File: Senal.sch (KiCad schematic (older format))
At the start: 19 parts, among them IC1 AG849, IC2 AD5933, P1 GSG-RF-CONN, P2 GSG-RF-CONN, P3 CONN_02X04, P4 CONN_01X01, U1 AD8606

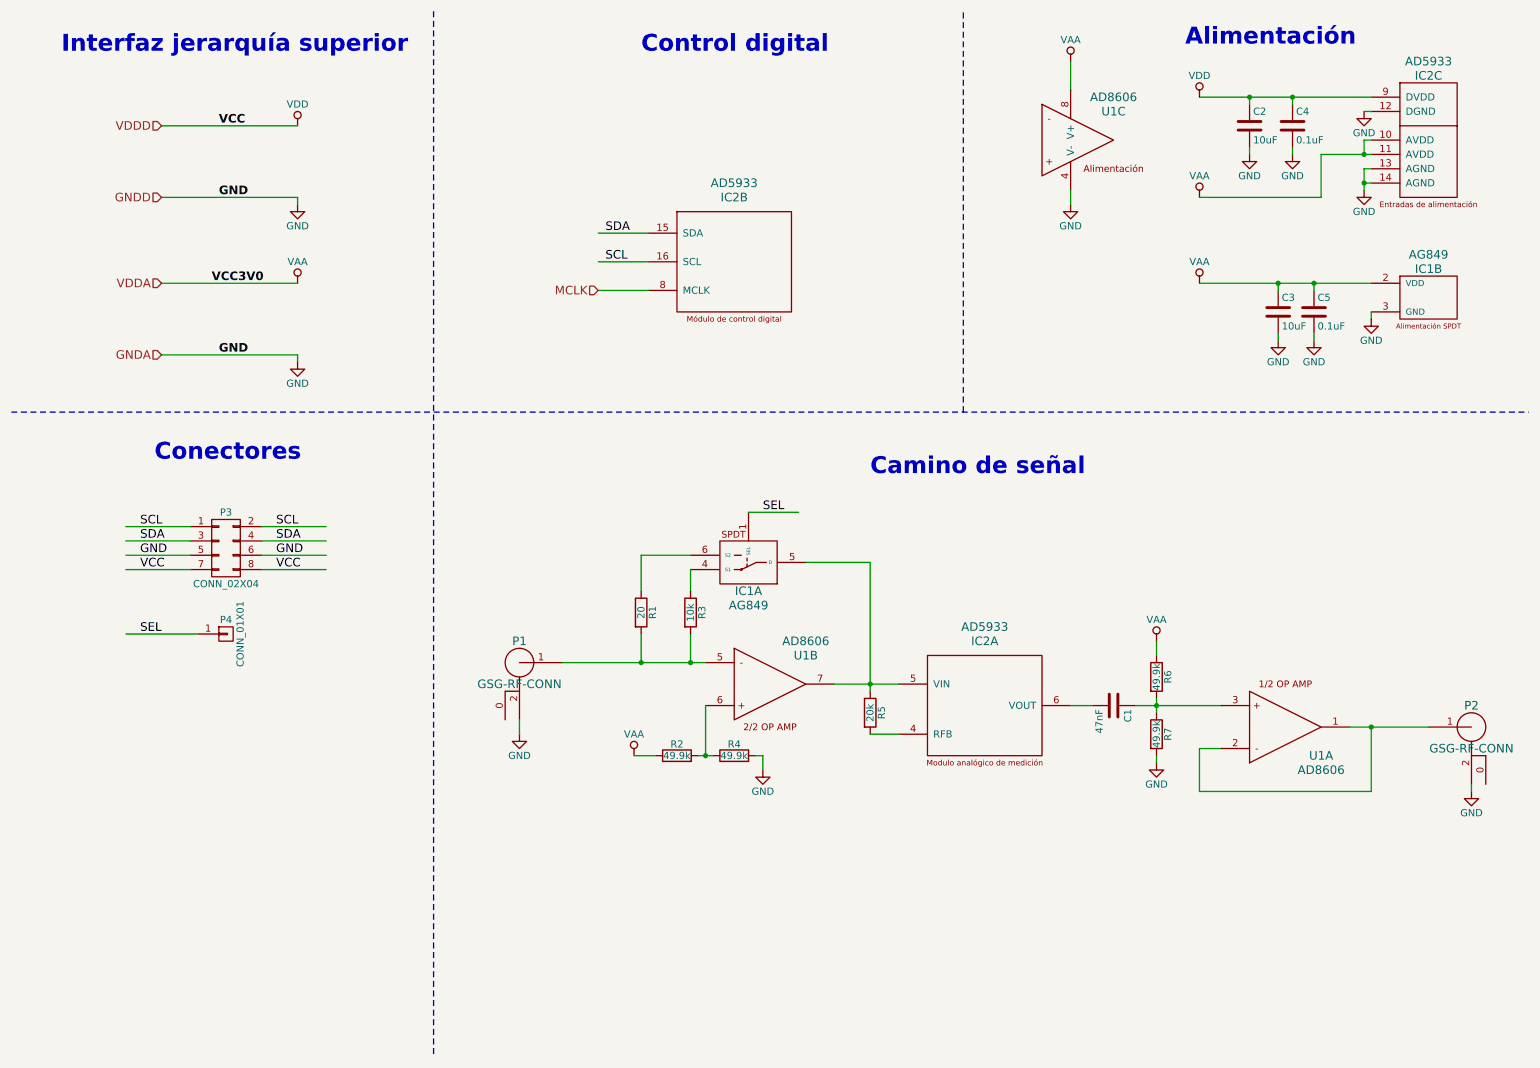
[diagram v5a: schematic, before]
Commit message: Footprints creados y linkeados. Listo para proceder al PCB. Todas las DRC dan OK
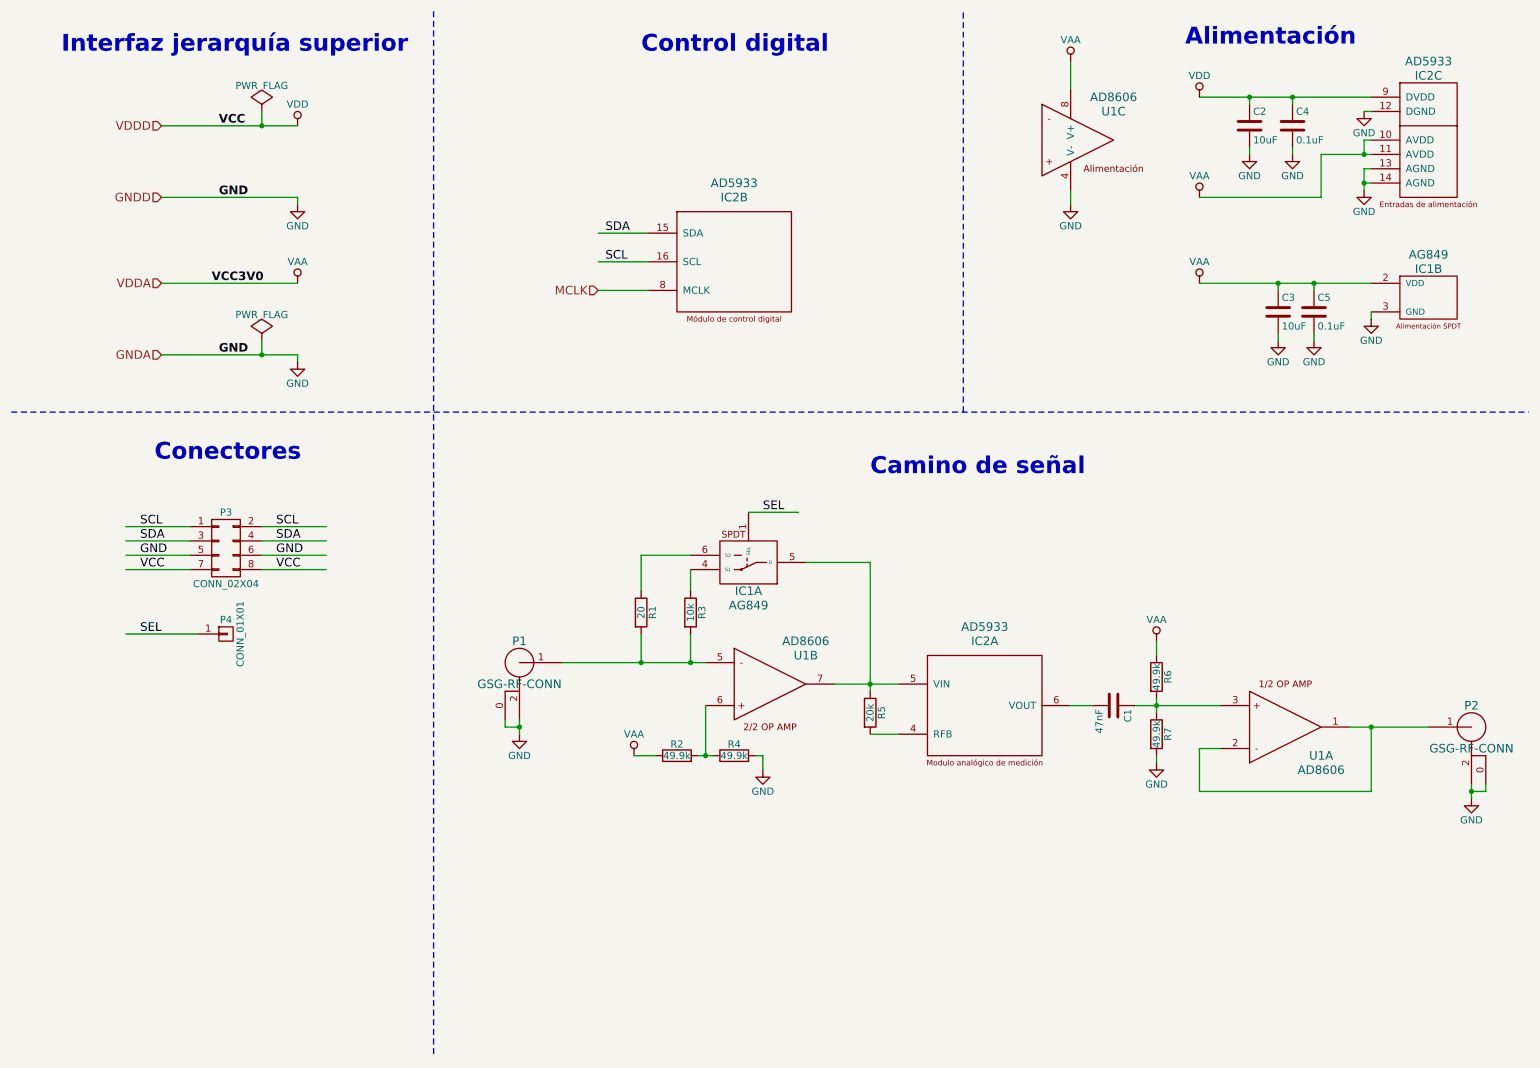
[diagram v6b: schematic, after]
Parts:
- C1, C2, C3, C4, C5: footprint (none) -> Capacitors_SMD:C_0805
- IC1: footprint (none) -> TO_SOT_Packages_SMD:SC-70-6
- IC2: footprint (none) -> Housings_SSOP:SSOP-16_5.3x6.2mm_Pitch0.65mm
- P1, P2: footprint (none) -> SMA_EDGE:SMA_EDGE
- P3: footprint (none) -> Pin_Headers:Pin_Header_Straight_2x04
- P4: footprint (none) -> Pin_Headers:Pin_Header_Straight_1x01
- R1, R2, R3, R4, R5, R6, R7: footprint (none) -> Resistors_SMD:R_0805
- U1: footprint (none) -> Housings_SSOP:MSOP-8_3x3mm_Pitch0.65mm
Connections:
- wire segments 68 -> 74
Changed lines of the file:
@@
 LIBS:PMOD_IA
 LIBS:SMA
+LIBS:sma2
 LIBS:proyectoDCI-cache
 EELAYER 25 0
@@
 F 0 "IC2" H 10450 1850 60  0000 C CNN
 F 1 "AD5933" H 10450 1950 60  0000 C CNN
-F 2 "" H 10450 1400 60  0001 C CNN
+F 2 "Housings_SSOP:SSOP-16_5.3x6.2mm_Pitch0.65mm" H 10450 1400 60  0001 C CNN
 F 3 "" H 10450 1400 60  0001 C CNN
 	3    10450 1400
@@
 F 0 "C2" H 9225 1400 50  0000 L CNN
 F 1 "10uF" H 9225 1200 50  0000 L CNN
-F 2 "" H 9238 1150 50  0000 C CNN
+F 2 "Capacitors_SMD:C_0805" H 9238 1150 50  0001 C CNN
 F 3 "" H 9200 1300 50  0000 C CNN
 	1    9200 1300
@@
 F 0 "C4" H 9525 1400 50  0000 L CNN
 F 1 "0.1uF" H 9525 1200 50  0000 L CNN
-F 2 "" H 9538 1150 50  0000 C CNN
+F 2 "Capacitors_SMD:C_0805" H 9538 1150 50  0001 C CNN
 F 3 "" H 9500 1300 50  0000 C CNN
 	1    9500 1300
@@
 F 0 "IC2" H 5600 2700 60  0000 C CNN
 F 1 "AD5933" H 5600 2800 60  0000 C CNN
-F 2 "" H 5600 2250 60  0001 C CNN
+F 2 "Housings_SSOP:SSOP-16_5.3x6.2mm_Pitch0.65mm" H 5600 2250 60  0001 C CNN
 F 3 "" H 5600 2250 60  0001 C CNN
 	2    5600 2250
@@
 F 0 "IC2" H 7350 5800 60  0000 C CNN
 F 1 "AD5933" H 7350 5900 60  0000 C CNN
-F 2 "" H 7350 5350 60  0001 C CNN
+F 2 "Housings_SSOP:SSOP-16_5.3x6.2mm_Pitch0.65mm" H 7350 5350 60  0001 C CNN
 F 3 "" H 7350 5350 60  0001 C CNN
 	1    7350 5350
@@
 F 0 "U1" H 8250 1600 60  0000 C CNN
 F 1 "AD8606" H 8250 1700 60  0000 C CNN
-F 2 "" H 8000 1400 60  0001 C CNN
+F 2 "Housings_SSOP:MSOP-8_3x3mm_Pitch0.65mm" H 8000 1400 60  0001 C CNN
 F 3 "" H 8000 1400 60  0001 C CNN
 	3    8000 1400
@@
 F 0 "IC1" H 10450 2700 60  0000 C CNN
 F 1 "AG849" H 10450 2800 60  0000 C CNN
-F 2 "" H 10450 2500 60  0001 C CNN
+F 2 "TO_SOT_Packages_SMD:SC-70-6" H 10450 2500 60  0001 C CNN
 F 3 "" H 10450 2500 60  0001 C CNN
 	2    10450 2500
@@
 F 0 "C3" H 9425 2700 50  0000 L CNN
 F 1 "10uF" H 9425 2500 50  0000 L CNN
-F 2 "" H 9438 2450 50  0000 C CNN
+F 2 "Capacitors_SMD:C_0805" H 9438 2450 50  0001 C CNN
 F 3 "" H 9400 2600 50  0000 C CNN
 	1    9400 2600
@@
 F 0 "C5" H 9675 2700 50  0000 L CNN
 F 1 "0.1uF" H 9675 2500 50  0000 L CNN
-F 2 "" H 9688 2450 50  0000 C CNN
+F 2 "Capacitors_SMD:C_0805" H 9688 2450 50  0001 C CNN
 F 3 "" H 9650 2600 50  0000 C CNN
 	1    9650 2600
@@
 F 0 "U1" H 9700 5700 60  0000 C CNN
 F 1 "AD8606" H 9700 5800 60  0000 C CNN
-F 2 "" H 9450 5500 60  0001 C CNN
+F 2 "Housings_SSOP:MSOP-8_3x3mm_Pitch0.65mm" H 9450 5500 60  0001 C CNN
 F 3 "" H 9450 5500 60  0001 C CNN
 	1    9450 5500
@@
 F 0 "U1" H 6100 5400 60  0000 C CNN
 F 1 "AD8606" H 6100 5500 60  0000 C CNN
-F 2 "" H 5850 5200 60  0001 C CNN
+F 2 "Housings_SSOP:MSOP-8_3x3mm_Pitch0.65mm" H 5850 5200 60  0001 C CNN
 F 3 "" H 5850 5200 60  0001 C CNN
 	2    5850 5200
@@
 F 0 "R5" V 6630 5400 50  0000 C CNN
 F 1 "20k" V 6550 5400 50  0000 C CNN
-F 2 "" V 6480 5400 50  0000 C CNN
+F 2 "Resistors_SMD:R_0805" V 6480 5400 50  0001 C CNN
 F 3 "" H 6550 5400 50  0000 C CNN
 	1    6550 5400
@@
 F 0 "R6" V 8630 5150 50  0000 C CNN
 F 1 "49.9k" V 8550 5150 50  0000 C CNN
-F 2 "" V 8480 5150 50  0000 C CNN
+F 2 "Resistors_SMD:R_0805" V 8480 5150 50  0001 C CNN
 F 3 "" H 8550 5150 50  0000 C CNN
 	1    8550 5150
@@
 F 0 "R7" V 8630 5550 50  0000 C CNN
 F 1 "49.9k" V 8550 5550 50  0000 C CNN
-F 2 "" V 8480 5550 50  0000 C CNN
+F 2 "Resistors_SMD:R_0805" V 8480 5550 50  0001 C CNN
 F 3 "" H 8550 5550 50  0000 C CNN
 	1    8550 5550
@@
 F 0 "C1" H 8275 5450 50  0000 L CNN
 F 1 "47nF" H 8275 5250 50  0000 L CNN
-F 2 "" H 8288 5200 50  0000 C CNN
+F 2 "Capacitors_SMD:C_0805" H 8288 5200 50  0001 C CNN
 F 3 "" H 8250 5350 50  0000 C CNN
 	1    8250 5350
@@
 F 0 "P2" H 10750 5650 60  0000 C CNN
 F 1 "GSG-RF-CONN" H 10750 5350 60  0000 C CNN
-F 2 "" H 10750 5500 60  0000 C CNN
+F 2 "SMA_EDGE:SMA_EDGE" H 10750 5500 60  0001 C CNN
 F 3 "" H 10750 5500 60  0000 C CNN
 	1    10750 5500
@@
 L GND #PWR012
 U 1 1 582FC324
-P 10750 5950
-F 0 "#PWR012" H 10750 5700 50  0001 C CNN
-F 1 "GND" H 10750 5800 50  0000 C CNN
-F 2 "" H 10750 5950 50  0000 C CNN
-F 3 "" H 10750 5950 50  0000 C CNN
-	1    10750 5950
+P 10750 6000
+F 0 "#PWR012" H 10750 5750 50  0001 C CNN
+F 1 "GND" H 10750 5850 50  0000 C CNN
+F 2 "" H 10750 6000 50  0000 C CNN
+F 3 "" H 10750 6000 50  0000 C CNN
+	1    10750 6000
 	1    0    0    -1
 $EndComp
@@
 F 0 "R2" V 5280 5700 50  0000 C CNN
 F 1 "49.9k" V 5200 5700 50  0000 C CNN
-F 2 "" V 5130 5700 50  0000 C CNN
+F 2 "Resistors_SMD:R_0805" V 5130 5700 50  0001 C CNN
 F 3 "" H 5200 5700 50  0000 C CNN
 	1    5200 5700
@@
 F 0 "R4" V 5680 5700 50  0000 C CNN
 F 1 "49.9k" V 5600 5700 50  0000 C CNN
-F 2 "" V 5530 5700 50  0000 C CNN
+F 2 "Resistors_SMD:R_0805" V 5530 5700 50  0001 C CNN
 F 3 "" H 5600 5700 50  0000 C CNN
 	1    5600 5700
@@
 F 0 "P1" H 4100 5200 60  0000 C CNN
 F 1 "GSG-RF-CONN" H 4100 4900 60  0000 C CNN
-F 2 "" H 4100 5050 60  0000 C CNN
+F 2 "SMA_EDGE:SMA_EDGE" H 4100 5050 60  0001 C CNN
 F 3 "" H 4100 5050 60  0000 C CNN
 	1    4100 5050
@@
 F 0 "IC1" H 5700 4550 60  0000 C CNN
 F 1 "AG849" H 5700 4650 60  0000 C CNN
-F 2 "" H 5700 4350 60  0001 C CNN
+F 2 "TO_SOT_Packages_SMD:SC-70-6" H 5700 4350 60  0001 C CNN
 F 3 "" H 5700 4350 60  0001 C CNN
 	1    5700 4350
@@
 F 0 "R3" V 5375 4700 50  0000 C CNN
 F 1 "10k" V 5295 4700 50  0000 C CNN
-F 2 "" V 5225 4700 50  0000 C CNN
+F 2 "Resistors_SMD:R_0805" V 5225 4700 50  0001 C CNN
 F 3 "" H 5295 4700 50  0000 C CNN
 	1    5295 4700
@@
 F 0 "R1" V 5030 4700 50  0000 C CNN
 F 1 "20" V 4950 4700 50  0000 C CNN
-F 2 "" V 4880 4700 50  0000 C CNN
+F 2 "Resistors_SMD:R_0805" V 4880 4700 50  0001 C CNN
 F 3 "" H 4950 4700 50  0000 C CNN
 	1    4950 4700
@@
 Connection ~ 10050 5500
 Wire Wire Line
-	10750 5900 10750 5950
+	10750 5900 10750 6000
 Connection ~ 6550 5200
 Wire Wire Line
@@
 F 0 "P3" H 2050 4500 50  0000 C CNN
 F 1 "CONN_02X04" H 2050 4000 50  0000 C CNN
-F 2 "" H 2050 3050 50  0000 C CNN
+F 2 "Pin_Headers:Pin_Header_Straight_2x04" H 2050 3050 50  0001 C CNN
 F 3 "" H 2050 3050 50  0000 C CNN
 	1    2050 4250
@@
 F 0 "P4" H 2050 4950 50  0000 C CNN
 F 1 "CONN_01X01" V 2150 4850 50  0000 C CNN
-F 2 "" H 2050 4850 50  0000 C CNN
+F 2 "Pin_Headers:Pin_Header_Straight_1x01" H 2050 4850 50  0001 C CNN
 F 3 "" H 2050 4850 50  0000 C CNN
 	1    2050 4850
@@
 Text Notes 1550 3650 0    118  ~ 24
 Conectores
+Wire Wire Line
+	4000 5450 4000 5500
+Wire Wire Line
+	4000 5500 4100 5500
+Connection ~ 4100 5500
+Wire Wire Line
+	10850 5900 10850 5950
+Wire Wire Line
+	10850 5950 10750 5950
+Connection ~ 10750 5950
+$Comp
+L PWR_FLAG #FLG023
+U 1 1 5838713B
+P 2300 1200
+F 0 "#FLG023" H 2300 1295 50  0001 C CNN
+F 1 "PWR_FLAG" H 2300 1380 50  0000 C CNN
+F 2 "" H 2300 1200 50  0000 C CNN
+F 3 "" H 2300 1200 50  0000 C CNN
+	1    2300 1200
+	1    0    0    -1
+$EndComp
+Wire Wire Line
+	2300 1200 2300 1300
+Connection ~ 2300 1300
+$Comp
+L PWR_FLAG #FLG024
+U 1 1 58387656
+P 2300 2800
+F 0 "#FLG024" H 2300 2895 50  0001 C CNN
+F 1 "PWR_FLAG" H 2300 2980 50  0000 C CNN
+F 2 "" H 2300 2800 50  0000 C CNN
+F 3 "" H 2300 2800 50  0000 C CNN
+	1    2300 2800
+	1    0    0    -1
+$EndComp
+Wire Wire Line
+	2300 2800 2300 2900
+Connection ~ 2300 2900
 $EndSCHEMATC
